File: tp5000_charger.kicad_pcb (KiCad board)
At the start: 2 copper layers, 41 x 30 mm, 23 parts, among them J1 VIN, J2 GND, J3 VOUT, J4 GND, J5 BAT+, J6 BAT-, P1 USB_C_Plug_USB2.0, U1 TP5000, U2 DW01, U3 FS8205A

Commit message: pcb design V1.1
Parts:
- removed P1: USB_C_Plug_USB2.0, Connector_USB:USB_C_Receptacle_HRO_TYPE-C-31-M-12
- added H1: Mounting, MountingHole:MountingHole_2.7mm_M2.5_DIN965_Pad, F.Cu at (86.2, 110.0)
- added H2: Mounting, MountingHole:MountingHole_2.7mm_M2.5_DIN965_Pad, F.Cu at (86.2, 134.5)
- added H3: Mounting, MountingHole:MountingHole_2.7mm_M2.5_DIN965_Pad, F.Cu at (113.2, 110.0)
- added H4: Mounting, MountingHole:MountingHole_2.7mm_M2.5_DIN965_Pad, F.Cu at (113.2, 134.5)
- added J7: USB_C_Receptacle_USB2.0, Connector_USB:USB_C_Receptacle_Palconn_UTC16-G, F.Cu at (87.5, 122.2)
- added R5: 10k, Resistor_SMD:R_0805_2012Metric, F.Cu at (98.0, 115.2)
- C1, C3, C5: footprint Capacitor_Tantalum_SMD:CP_EIA-3216-12_Kemet-S_Pad1.58x1.35mm_HandSolder -> Capacitor_Tantalum_SMD:CP_EIA-3216-12_Kemet-S
- C2, C4: footprint Capacitor_SMD:C_0805_2012Metric_Pad1.18x1.45mm_HandSolder -> Capacitor_SMD:C_0805_2012Metric
- D2, D3: footprint LED_SMD:LED_0805_2012Metric_Pad1.15x1.40mm_HandSolder -> LED_SMD:LED_0805_2012Metric
- J1, J2, J3, J4, J5, J6: footprint TestPoint:TestPoint_THTPad_4.0x4.0mm_Drill2.0mm -> TestPoint:TestPoint_THTPad_2.5x2.5mm_Drill1.2mm
- L1: footprint Inductor_SMD:L_Taiyo-Yuden_NR-50xx_HandSoldering -> Inductor_SMD:L_Taiyo-Yuden_NR-50xx
- R2: value 10k -> 1k; footprint Resistor_SMD:R_0805_2012Metric_Pad1.20x1.40mm_HandSolder -> Resistor_SMD:R_0805_2012Metric
- R3, R4: footprint Resistor_SMD:R_0805_2012Metric_Pad1.20x1.40mm_HandSolder -> Resistor_SMD:R_0805_2012Metric
- moved C5 14.5 mm to (107.2, 114.0), turned to 180 degrees
- moved R3 11.8 mm to (104.2, 116.8), turned to 180 degrees
- moved J3 8.81 mm to (113.8, 115.0)
- moved J2 8.53 mm to (113.8, 129.5)
- moved J5 7.95 mm to (113.8, 119.2)
- moved J6 7.75 mm to (113.8, 125.2)
- moved U2 7.11 mm to (108.0, 118.1)
- moved U3 7.09 mm to (108.0, 124.9)
- moved R4 6.35 mm to (104.2, 119.5), turned to 0 degrees
- moved R2 6.01 mm to (97.0, 112.2), turned to 0 degrees
- moved D3 5.30 mm to (95.8, 115.2)
- moved L1 5.17 mm to (98.3, 126.2)
- moved J1 5.06 mm to (85.2, 115.0)
- moved C4 5.02 mm to (105.0, 122.5)
- moved J4 4.56 mm to (85.2, 129.5)
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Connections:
- R2 pad 2: GND -> VIN
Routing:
- net GND: track 45.4 -> 20.7 mm, vias 22 -> 12
- net Net-(R3-Pad1): track 11.4 -> 4.35 mm
- net VIN: track 30.8 -> 37.7 mm
- net B+: track 40.7 -> 34.8 mm
- net Net-(D1-Pad1): track 18.2 -> 12.6 mm
- net Net-(R5-Pad1): track 0.00 -> 3.97 mm
- net Net-(D3-Pad1): track 5.87 -> 2.45 mm
- net B-: track 24.7 -> 21.4 mm, vias 2 -> 0
- net Net-(J7-PadB6): track 0.00 -> 3.21 mm
- net Net-(D2-Pad2): track 7.02 -> 4.39 mm
- net Net-(C3-Pad1): track 15.0 -> 12.6 mm
- net Net-(D2-Pad1): track 4.33 -> 2.56 mm
- net Net-(C4-Pad1): track 9.67 -> 8.76 mm, vias 0 -> 2
- net Net-(P1-PadA6): track 0.50 -> 0.00 mm
- net Net-(J7-PadA6): track 0.00 -> 0.50 mm
- removed copper zone on F.Cu, net VIN
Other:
- board size 41 x 30 mm -> 33.5 x 31 mm
- board text added: "Ri"
- board text added: "Rsel"
- board text removed: "3.0V - 3.6V R1 1Ω100mA 0.2Ω500mA 0.1Ω1000mA"
- board text removed: "TP5000 LiFePo4 Charger"

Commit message: layout smaller
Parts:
- removed H3, H4: Mounting, MountingHole:MountingHole_2.7mm_M2.5_DIN965_Pad
- moved J4 20.4 mm to (95.2, 111.8)
- moved D3 8.31 mm to (103.1, 111.2), turned to 180 degrees
- moved D2 7.12 mm to (99.4, 111.2), turned to 0 degrees
- moved J1 6.82 mm to (91.2, 111.8)
- moved H2 5.00 mm to (86.2, 129.5)
- moved C1 3.73 mm to (93.6, 115.2), turned to 0 degrees
- moved R2 2.65 mm to (99.3, 113.5), turned to 180 degrees
- moved H1 2.50 mm to (86.2, 112.5)
- moved J3 1.50 mm to (113.8, 113.5)
- moved J5 1.50 mm to (113.8, 117.8)
- moved J7 1.27 mm to (87.2, 121.0)
- moved J2 1.00 mm to (113.8, 128.5)
- moved J6 1.00 mm to (113.8, 124.2)
- moved R5 0.93 mm to (98.4, 116.0), turned to 180 degrees
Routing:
- net Net-(D3-Pad1): track 2.45 -> 13.3 mm
- net Net-(D2-Pad1): track 2.56 -> 9.82 mm, vias 0 -> 2
- net VIN: track 37.7 -> 31.2 mm
- net B+: track 34.8 -> 32.1 mm
- net GND: track 20.7 -> 18.9 mm
- net Net-(J7-PadA6): track 0.50 -> 1.98 mm
- net Net-(R5-Pad1): track 3.97 -> 5.21 mm
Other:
- board size 33.5 x 31 mm -> 33 x 23.5 mm
- board text added: "Ri: 1=100mA 0.2=500mA 0.1=1000mA"
- board text added: "Rsel: 10k=4.2V open=3.6V"
- board text added: "TP5000 Lithium Charger V1.1"

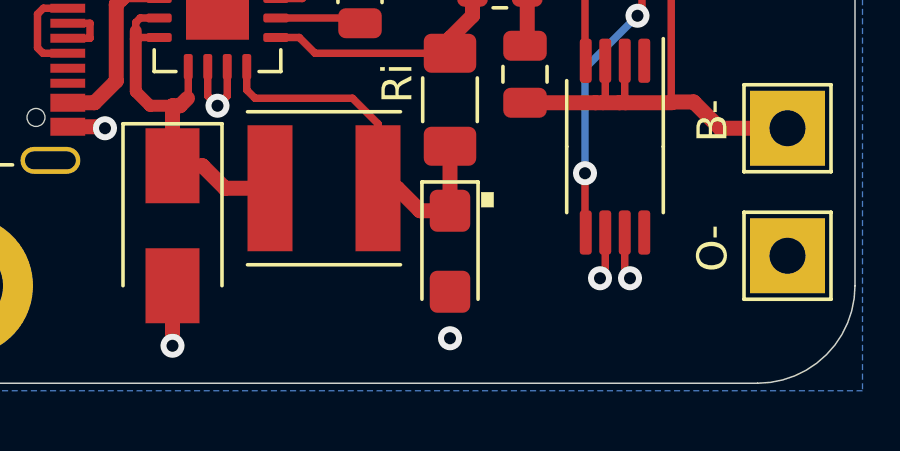
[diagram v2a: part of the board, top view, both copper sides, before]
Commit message: gnd connection c3
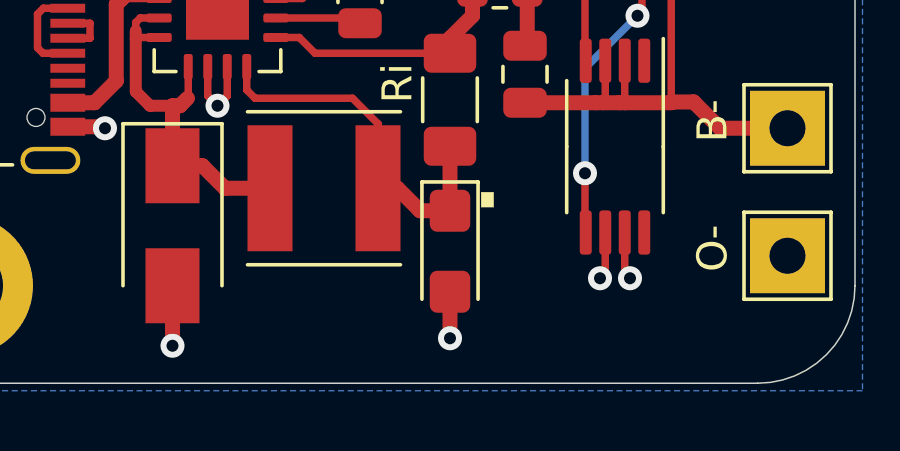
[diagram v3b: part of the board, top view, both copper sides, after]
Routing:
- net GND: track 18.9 -> 20.5 mm

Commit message: version number 1.2
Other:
- board text added: "TP5000 Lithium Charger V1.2"
- board text removed: "TP5000 Lithium Charger V1.1"
